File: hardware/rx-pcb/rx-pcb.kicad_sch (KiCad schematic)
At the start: 1 part, among them U1 STM32WB05KZVx

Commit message: Signed-off-by: a-conspiracy-theory <rdwitt1340@gmail.com>
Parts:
- removed U1: STM32WB05KZVx, Package_DFN_QFN:QFN-32-1EP_5x5mm_P0.5mm_EP3.7x3.7mm, symbol MCU_ST_STM32WB:STM32WB05KZVx
- added C1, C10, C3, C6, C8: 100n, Capacitor_SMD:C_0805_2012Metric_Pad1.18x1.45mm_HandSolder, symbol Device:C
- added C11: 220n, Capacitor_SMD:C_0805_2012Metric_Pad1.18x1.45mm_HandSolder, symbol Device:C
- added C12, C13: 20p, Capacitor_SMD:C_0805_2012Metric_Pad1.18x1.45mm_HandSolder, symbol Device:C
- added C2, C9: 4.7uF, Capacitor_SMD:C_0805_2012Metric_Pad1.18x1.45mm_HandSolder, symbol Device:C
- added C4: 1u, Capacitor_SMD:C_0805_2012Metric_Pad1.18x1.45mm_HandSolder, symbol Device:C
- added C5, C7: 3p, Capacitor_SMD:C_0805_2012Metric_Pad1.18x1.45mm_HandSolder, symbol Device:C
- added J1: Conn_01x05_Pin, Connector_PinHeader_2.54mm:PinHeader_1x05_P2.54mm_Vertical, symbol Connector:Conn_01x05_Pin
- added J2: Conn_01x04_Pin, Connector_PinSocket_2.54mm:PinSocket_1x04_P2.54mm_Vertical, symbol Connector:Conn_01x04_Pin
- added L1: 10uH, Inductor_SMD:L_0805_2012Metric_Pad1.05x1.20mm_HandSolder, symbol Device:L
- added L2: 22nH, Inductor_SMD:L_0805_2012Metric_Pad1.05x1.20mm_HandSolder, symbol Device:L
- added SW1: SW_SPST, Button_Switch_THT:SW_PUSH_6mm, symbol Switch:SW_SPST
- added U2: STM32WB05KZV6TR, easyeda:UFQFN-32_L5.0-W5.0-P0.50-TL-EP3.5, symbol easyeda:STM32WB05KZV6TR
- added X1: Q22FA12800025, easyeda:CRYSTAL-SMD_4P-L2.0-W1.6-BL, symbol easyeda:Q22FA12800025
- added X2: ABS07-32.768KHZ-1-T, easyeda:OSC-SMD_2P-L3.2-W1.5, symbol easyeda:ABS07-32.768KHZ-1-T
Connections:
- new net: L1.2, L2.1
- new net 3V3: J1.1 (Pin_1), J2.2 (Pin_2)
- new net GND: C1.2, C10.2, C11.2, C12.2, C13.2, C2.2, C3.2, C4.2, C5.2, C6.2, C7.2, C8.2, C9.2, J1.3 (Pin_3), J2.1 (Pin_1), SW1.1 (A), U2.26 (VSS), U2.33 (GND), X1.2 (GND), X1.4 (GND)
- new net RF1: U2.14 (RF1)
- new net VCAP: C11.1, U2.28 (VCAP)
- new net VCC: C10.1, C4.1, C5.1, C6.1, C7.1, C8.1, C9.1, U2.13 (VDD2), U2.15 (VDDRF), U2.24 (VDDSD), U2.32 (VDD1)
- new net hsei: U2.17 (OSCIN), X1.1
- new net hseo: U2.16 (OSCOUT), X1.3
- new net lsei: C12.1, U2.20 (PB13/RCC_OSC32_IN), X2.1 (OSC1)
- new net lseo: C13.1, U2.21 (PB12/RCC_OSC32_OUT), X2.2 (OSC2)
- new net rst: C1.1, J1.5 (Pin_5), SW1.2 (B), U2.29 (RSTN)
- new net swclk: J1.2 (Pin_2), U2.5 (PA3)
- new net swdio: J1.4 (Pin_4), U2.6 (PA2)
- new net uart_rx: J2.3 (Pin_3), U2.22 (PB7)
- new net uart_tx: J2.4 (Pin_4), U2.23 (PB6)
- new net vfbsd: C2.1, C3.1, L1.1, U2.27 (VFBSD)
- new net vlxsd: L2.2, U2.25 (VLXSD)
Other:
- note added: "SWDebug"
- note added: "UART"

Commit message: RF work start
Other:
- added sheet PWR (untitled.kicad_sch)
- added sheet RF (untitled.kicad_sch)
- moved on the sheet: C1, C10, C11, C12, C13, C2, C3, C4, C5, C6, C7, C8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

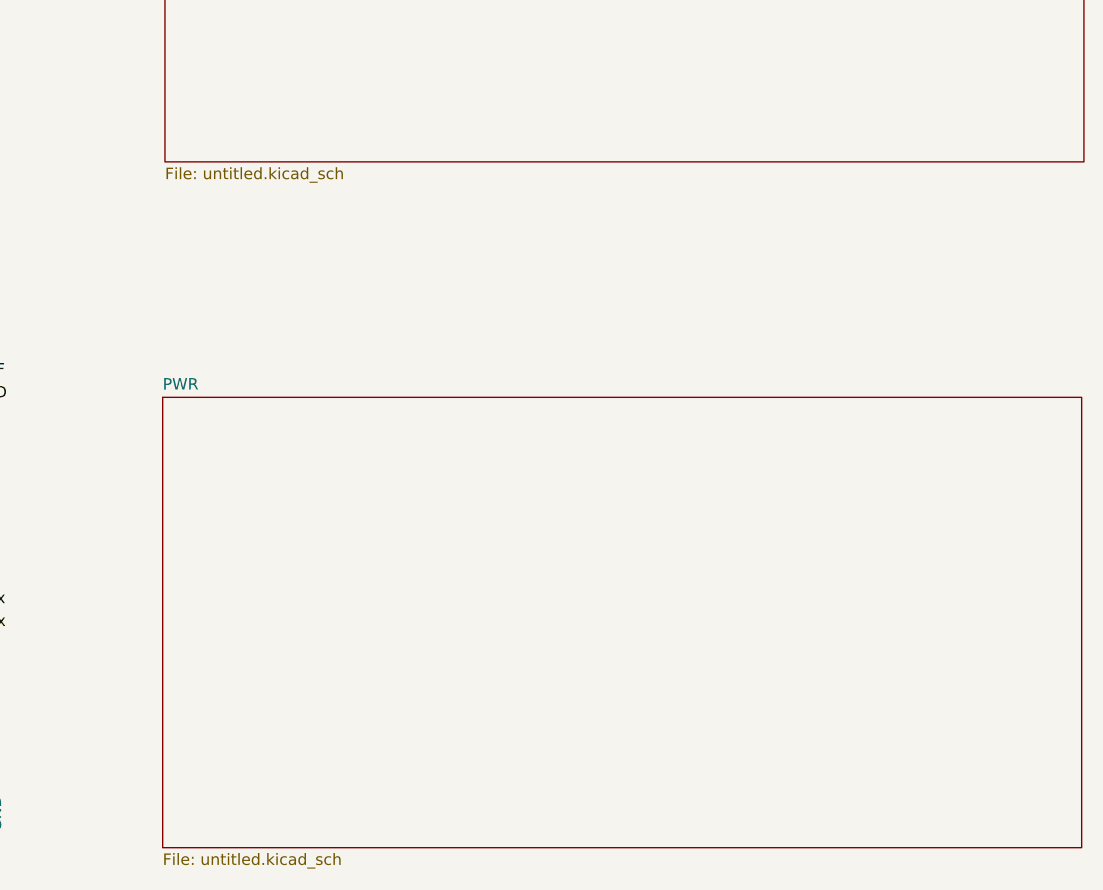
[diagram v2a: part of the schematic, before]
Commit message: minor board updates. added the MLPF-WB chip for stm impedance matching
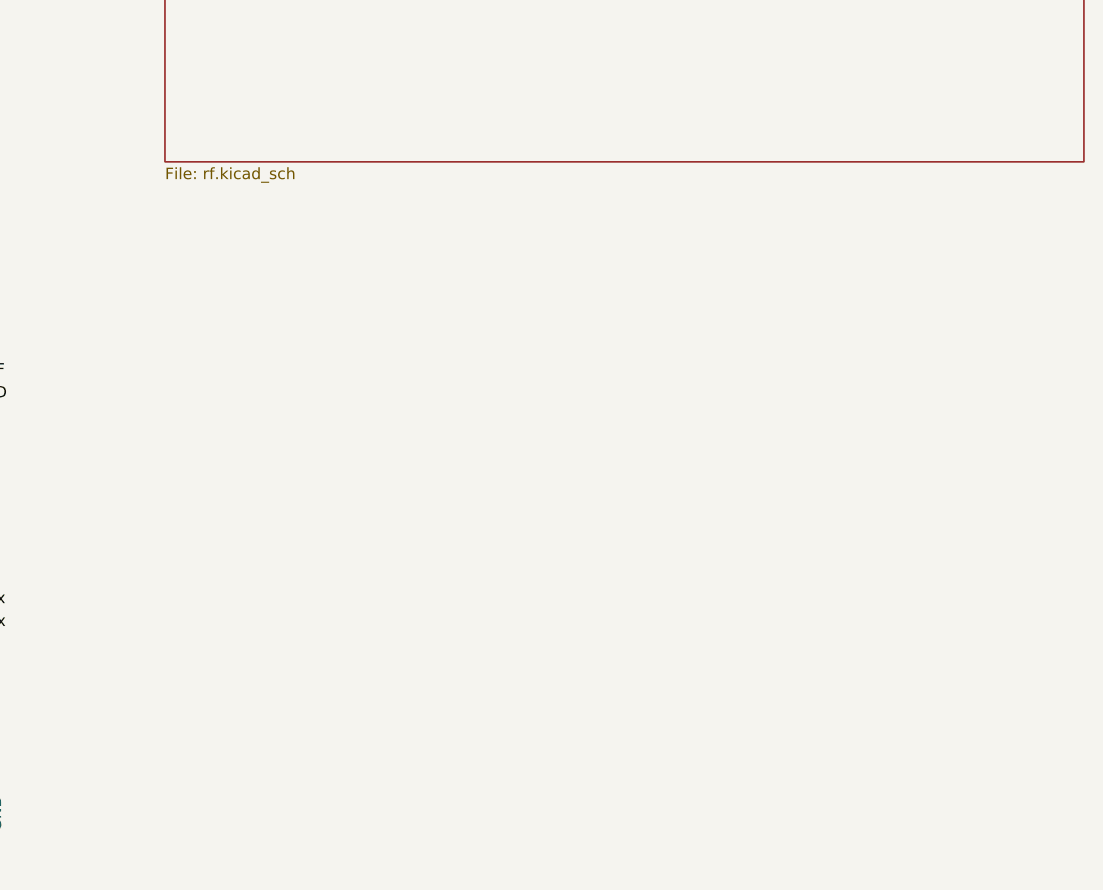
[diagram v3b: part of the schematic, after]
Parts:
- J2: footprint Connector_PinSocket_2.54mm:PinSocket_1x04_P2.54mm_Vertical -> Connector_PinHeader_2.54mm:PinHeader_1x04_P2.54mm_Vertical
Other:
- removed sheet PWR
- sheet RF: file untitled.kicad_sch -> rf.kicad_sch
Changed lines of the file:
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@@
 			)
 		)
-		(property "Footprint" "Connector_PinSocket_2.54mm:PinSocket_1x04_P2.54mm_Vertical"
+		(property "Footprint" "Connector_PinHeader_2.54mm:PinHeader_1x04_P2.54mm_Vertical"
 			(at 124.46 57.15 0)
 			(effects
@@
 	)
 	(sheet
-		(at 151.892 102.362)
-		(size 102.108 50.038)
+		(at 152.146 25.654)
+		(size 102.108 50.546)
 		(exclude_from_sim no)
 		(in_bom yes)
@@
 			(color 0 0 0 0.0000)
 		)
-		(property "Sheetname" "PWR"
-			(at 151.892 101.6504 0)
-			(effects
-				(font
-					(size 1.27 1.27)
-				)
-				(justify left bottom)
-			)
-		)
-		(property "Sheetfile" "untitled.kicad_sch"
-			(at 151.892 152.9846 0)
-			(effects
-				(font
-					(size 1.27 1.27)
-				)
-				(justify left top)
-			)
-		)
-		(instances
-			(project "rx-pcb"
-				(path "/9df8ddb8-545e-44cf-b4e7-941b19ec42ab"
-					(page "3")
-				)
-			)
-		)
-	)
-	(sheet
-		(at 152.146 25.654)
-		(size 102.108 50.546)
-		(exclude_from_sim no)
-		(in_bom yes)
-		(on_board yes)
-		(dnp no)
-		(fields_autoplaced yes)
-		(stroke
-			(width 0.1524)
-			(type solid)
-		)
-		(fill
-			(color 0 0 0 0.0000)
-		)
 		(property "Sheetname" "RF"
 			(at 152.146 24.9424 0)
@@
 			)
 		)
-		(property "Sheetfile" "untitled.kicad_sch"
+		(property "Sheetfile" "rf.kicad_sch"
 			(at 152.146 76.7846 0)
 			(effects

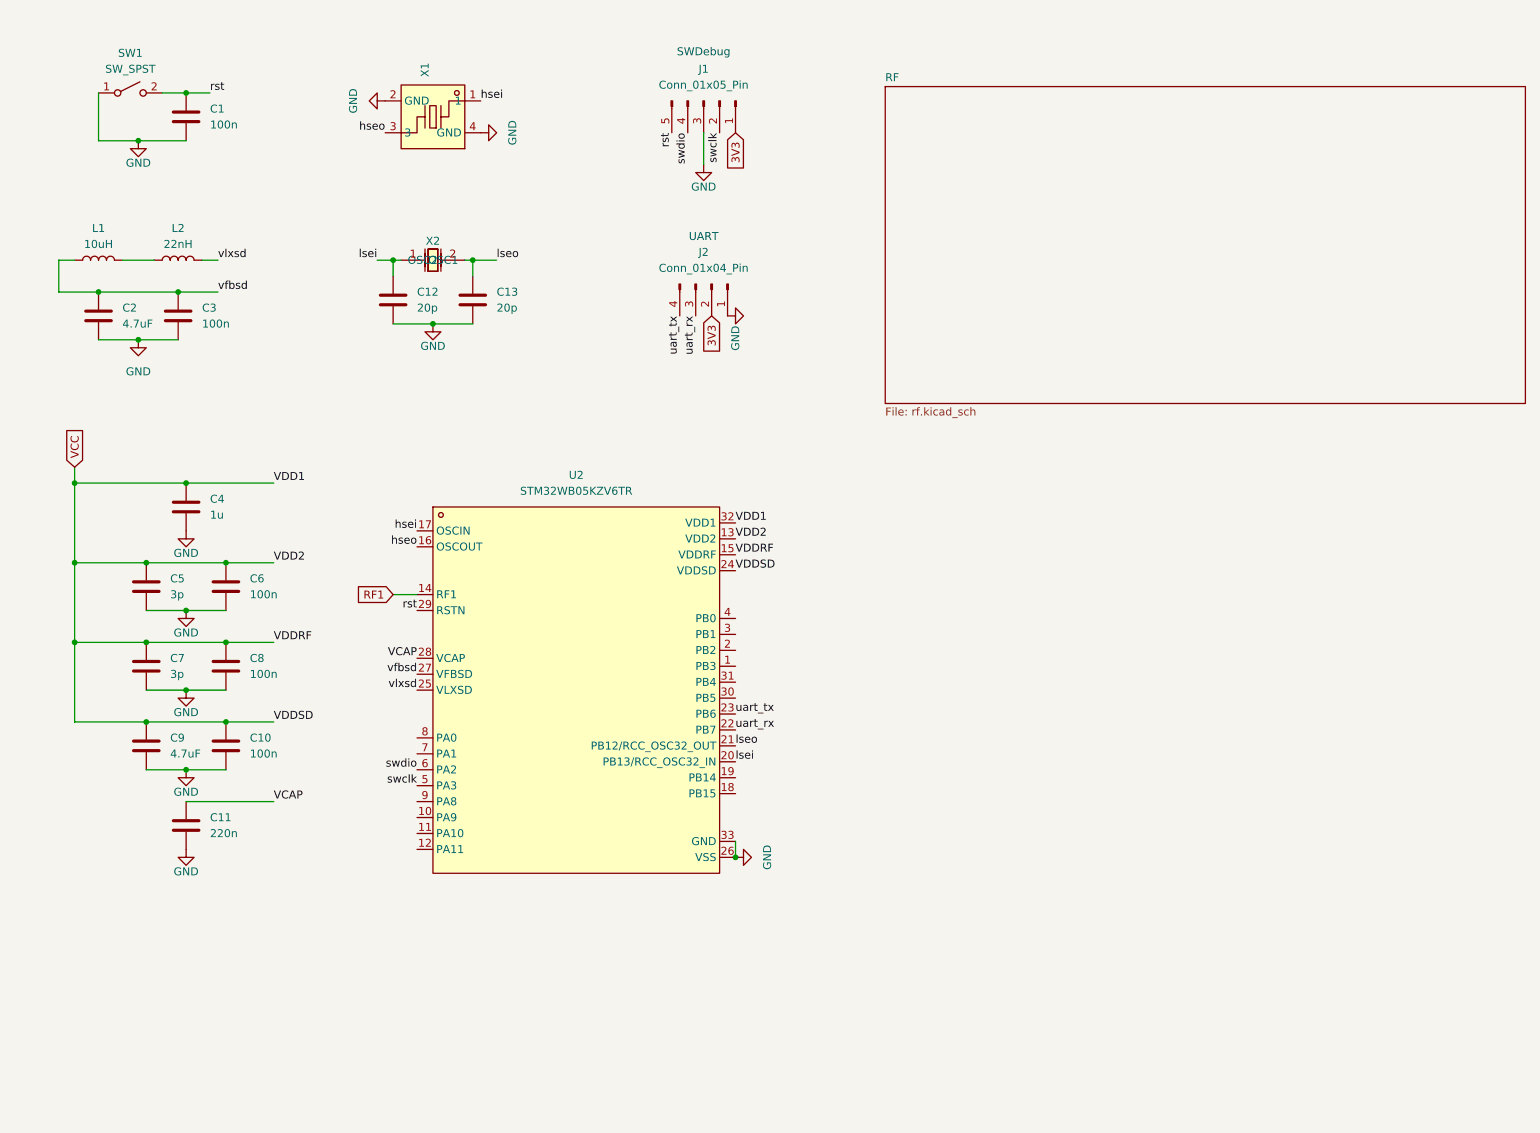
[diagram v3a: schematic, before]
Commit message: finished initial board. no sensors or power harvesting, but its programmable and bluetooth should work.
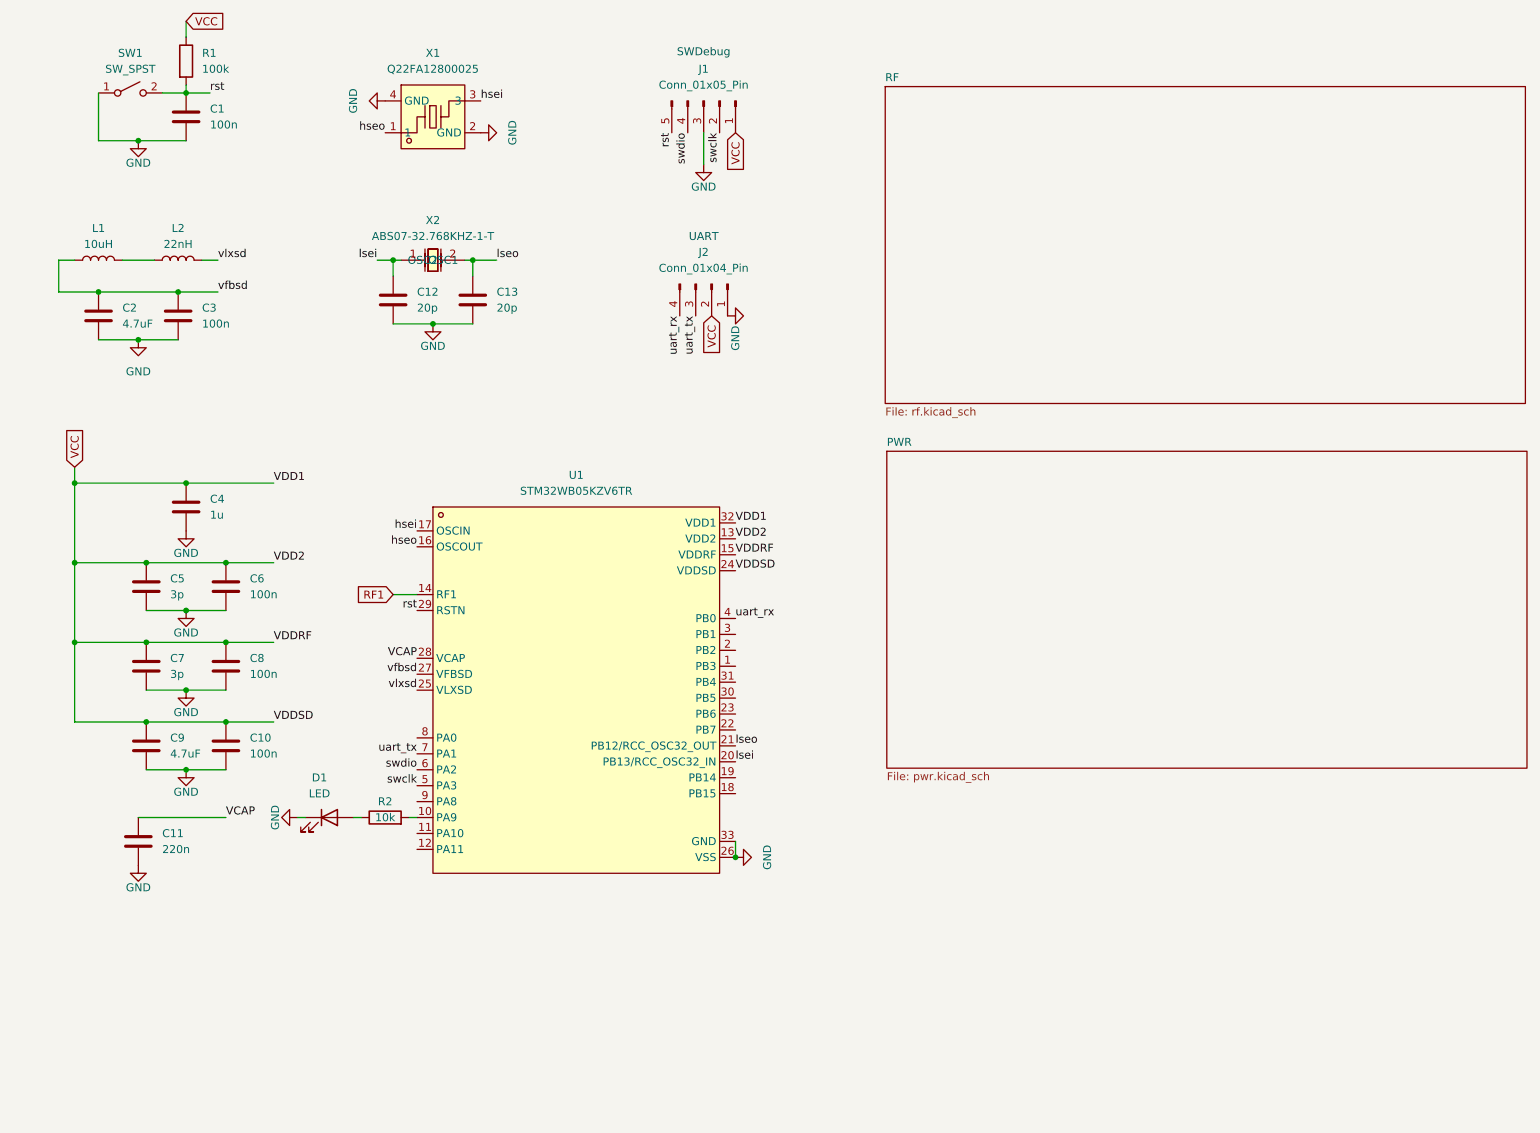
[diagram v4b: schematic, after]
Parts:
- removed U2: STM32WB05KZV6TR, easyeda:UFQFN-32_L5.0-W5.0-P0.50-TL-EP3.5, symbol easyeda:STM32WB05KZV6TR
- removed X1: Q22FA12800025, easyeda:CRYSTAL-SMD_4P-L2.0-W1.6-BL, symbol easyeda:Q22FA12800025
- removed X2: ABS07-32.768KHZ-1-T, easyeda:OSC-SMD_2P-L3.2-W1.5, symbol easyeda:ABS07-32.768KHZ-1-T
- added D1: LED, rx-parts:LED_0805_2012Metric_Pad1.15x1.40mm_HandSolder, symbol rx-parts:LED
- added R1: 100k, rx-parts:R_0805_2012Metric_Pad1.20x1.40mm_HandSolder, symbol rx-parts:R
- added R2: 10k, rx-parts:R_0805_2012Metric_Pad1.20x1.40mm_HandSolder, symbol rx-parts:R
- added U1: STM32WB05KZV6TR, rx-parts:UFQFN-32_L5.0-W5.0-P0.50-TL-EP3.5, symbol rx-parts:STM32WB05KZV6TR
- added X1: Q22FA12800025, rx-parts:CRYSTAL-SMD_4P-L2.0-W1.6-BL, symbol rx-parts:Q22FA12800025
- added X2: ABS07-32.768KHZ-1-T, rx-parts:OSC-SMD_2P-L3.2-W1.5, symbol rx-parts:ABS07-32.768KHZ-1-T
- C1, C10, C11, C12, C13, C2, C3, C4, C5, C6, C7, C8, C9: footprint Capacitor_SMD:C_0805_2012Metric_Pad1.18x1.45mm_HandSolder -> rx-parts:C_0805_2012Metric_Pad1.18x1.45mm_HandSolder; symbol Device:C -> rx-parts:C
- J1: footprint Connector_PinHeader_2.54mm:PinHeader_1x05_P2.54mm_Vertical -> rx-parts:PinHeader_1x05_P2.54mm_Vertical; symbol Connector:Conn_01x05_Pin -> rx-parts:Conn_01x05_Pin
- J2: footprint Connector_PinHeader_2.54mm:PinHeader_1x04_P2.54mm_Vertical -> rx-parts:PinHeader_1x04_P2.54mm_Vertical; symbol Connector:Conn_01x04_Pin -> rx-parts:Conn_01x04_Pin
- L1, L2: footprint Inductor_SMD:L_0805_2012Metric_Pad1.05x1.20mm_HandSolder -> rx-parts:L_0805_2012Metric_Pad1.05x1.20mm_HandSolder; symbol Device:L -> rx-parts:L
- SW1: footprint Button_Switch_THT:SW_PUSH_6mm -> rx-parts:SW_PUSH_6mm; symbol Switch:SW_SPST -> rx-parts:SW_SPST
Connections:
- net 3V3 is gone; now on net VCC: J1.1 (Pin_1), J2.2 (Pin_2)
- net GND: now also D1.1 (K), U1.26 (VSS), U1.33 (GND), X1.2 (GND), X1.4 (GND)
- net RF1: now also U1.14 (RF1)
- net VCAP: now also U1.28 (VCAP)
- net VCC: now also R1.1, U1.13 (VDD2), U1.15 (VDDRF), U1.24 (VDDSD), U1.32 (VDD1)
- net hsei: now also U1.17 (OSCIN), X1.3
- net hseo: now also U1.16 (OSCOUT), X1.1
- net lsei: now also U1.20 (PB13/RCC_OSC32_IN), X2.1 (OSC1)
- net lseo: now also U1.21 (PB12/RCC_OSC32_OUT), X2.2 (OSC2)
- net rst: now also R1.2, U1.29 (RSTN)
- net swclk: now also U1.5 (PA3)
- net swdio: now also U1.6 (PA2)
- net uart_rx: now also J2.4 (Pin_4), U1.4 (PB0); no longer J2.3 (Pin_3)
- net uart_tx: now also J2.3 (Pin_3), U1.7 (PA1); no longer J2.4 (Pin_4)
- net vfbsd: now also U1.27 (VFBSD)
- net vlxsd: now also U1.25 (VLXSD)
- new net: D1.2 (A), R2.1
- new net: R2.2, U1.10 (PA9)
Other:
- added sheet PWR (pwr.kicad_sch)
- moved on the sheet: C11

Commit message: updated bluetooth section to be in-line with filter datasheet. rearranged LFEX to allow I2C connection.
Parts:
- added U2: STS4L-AD1B-R3, easyeda2kicad:DFN-4_L1.5-W1.5-P0.80-TL-EP, symbol easyeda2kicad:STS4L-AD1B-R3
- renumbered C8 to C10, C9 to C11, C10 to C12, C11 to C13, C12 to C2, C13 to C3, C2 to C4, C3 to C5, C4 to C6, C5 to C7, C6 to C8, C7 to C9
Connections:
- net GND: now also U2.4 (VSS), U2.5 (EP)
- net VCC: now also U2.3 (VDD)
- net i2c_sda: now reaches U1.22 (PB7)
- net i2c_sda: now also U2.1 (SDA)
- net i2c_scl: now reaches U1.23 (PB6)
- net i2c_scl: now also U2.2 (SCL)

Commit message: finished V1 of receiver PCB. No power electronics yet.
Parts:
- added J4: Conn_01x04_Pin, rx-parts:PinHeader_1x04_P2.54mm_Vertical, symbol rx-parts:Conn_01x04_Pin
- added R3, R4: 100k, rx-parts:R_0805_2012Metric_Pad1.20x1.40mm_HandSolder, symbol rx-parts:R
- added U3: LMT70AYFQR, easyeda2kicad:DSBGA-4_L0.8-W0.8-R2-C2-P0.40-BL, symbol easyeda2kicad:LMT70AYFQR
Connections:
- net GND: now also J4.1 (Pin_1), U3.A1 (GND)
- net VCC: now also J4.2 (Pin_2), R3.1, R4.1, U3.A2 (VDD), U3.B2 (T_ON)
- net i2c_scl: now also J4.4 (Pin_4), R3.2
- net i2c_sda: now also J4.3 (Pin_3), R4.2
- net TMP_A: now reaches U1.8 (PA0)
- net TMP_A: now also U3.B1 (TAO)
